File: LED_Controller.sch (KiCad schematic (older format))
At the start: 27 parts, among them CON1 CONNECTOR, CON2 CONNECTOR, CON3 CONNECTOR, CON4 CONNECTOR, CON5 PWR_CON, CON6 AVR-ISP-10, CON7 AVR-ISP-6, IC1 ATMEGA328P-P, Q1 STS8DN3LLH5, Q2 STS8DN3LLH5, Q3 STS8DN3LLH5

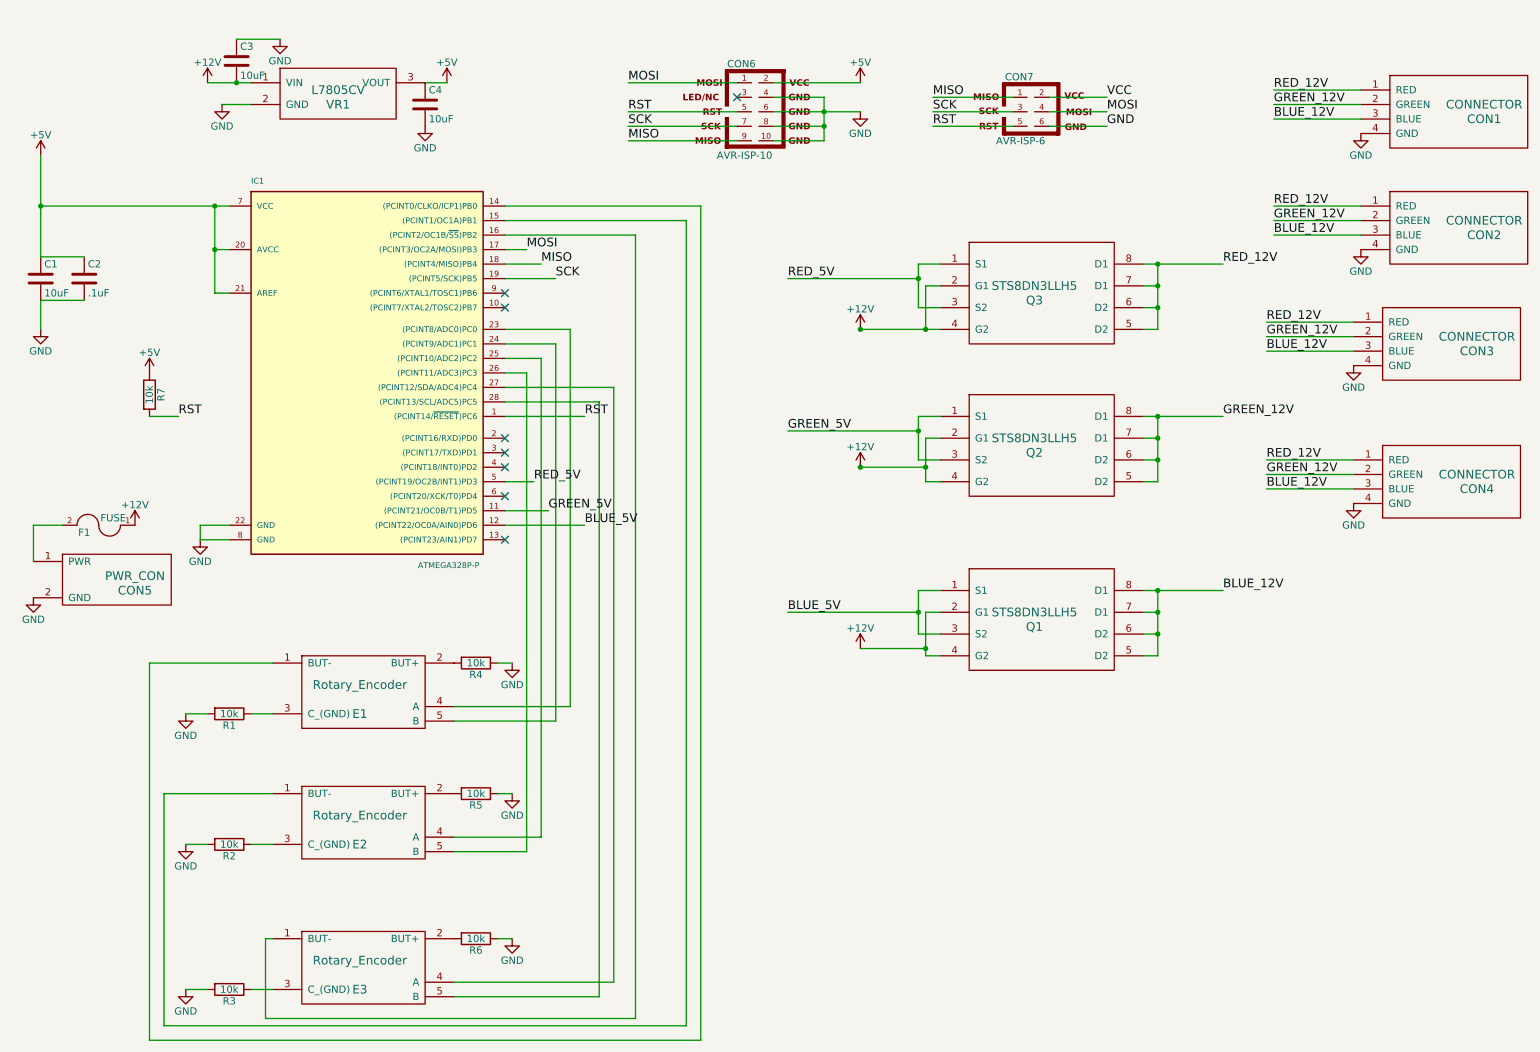
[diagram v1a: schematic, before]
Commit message: Changed to Common Anode, new status LEDs
Updated schematic to reflect common anode LED strip, instead of common
cathode.

Added indicator LEDs to 12V and 5V power supply.

Other minor routing changes. Still need to update footprint to make
rotary encoder pins larger and probably change the Atmega footprint to
the correct size.
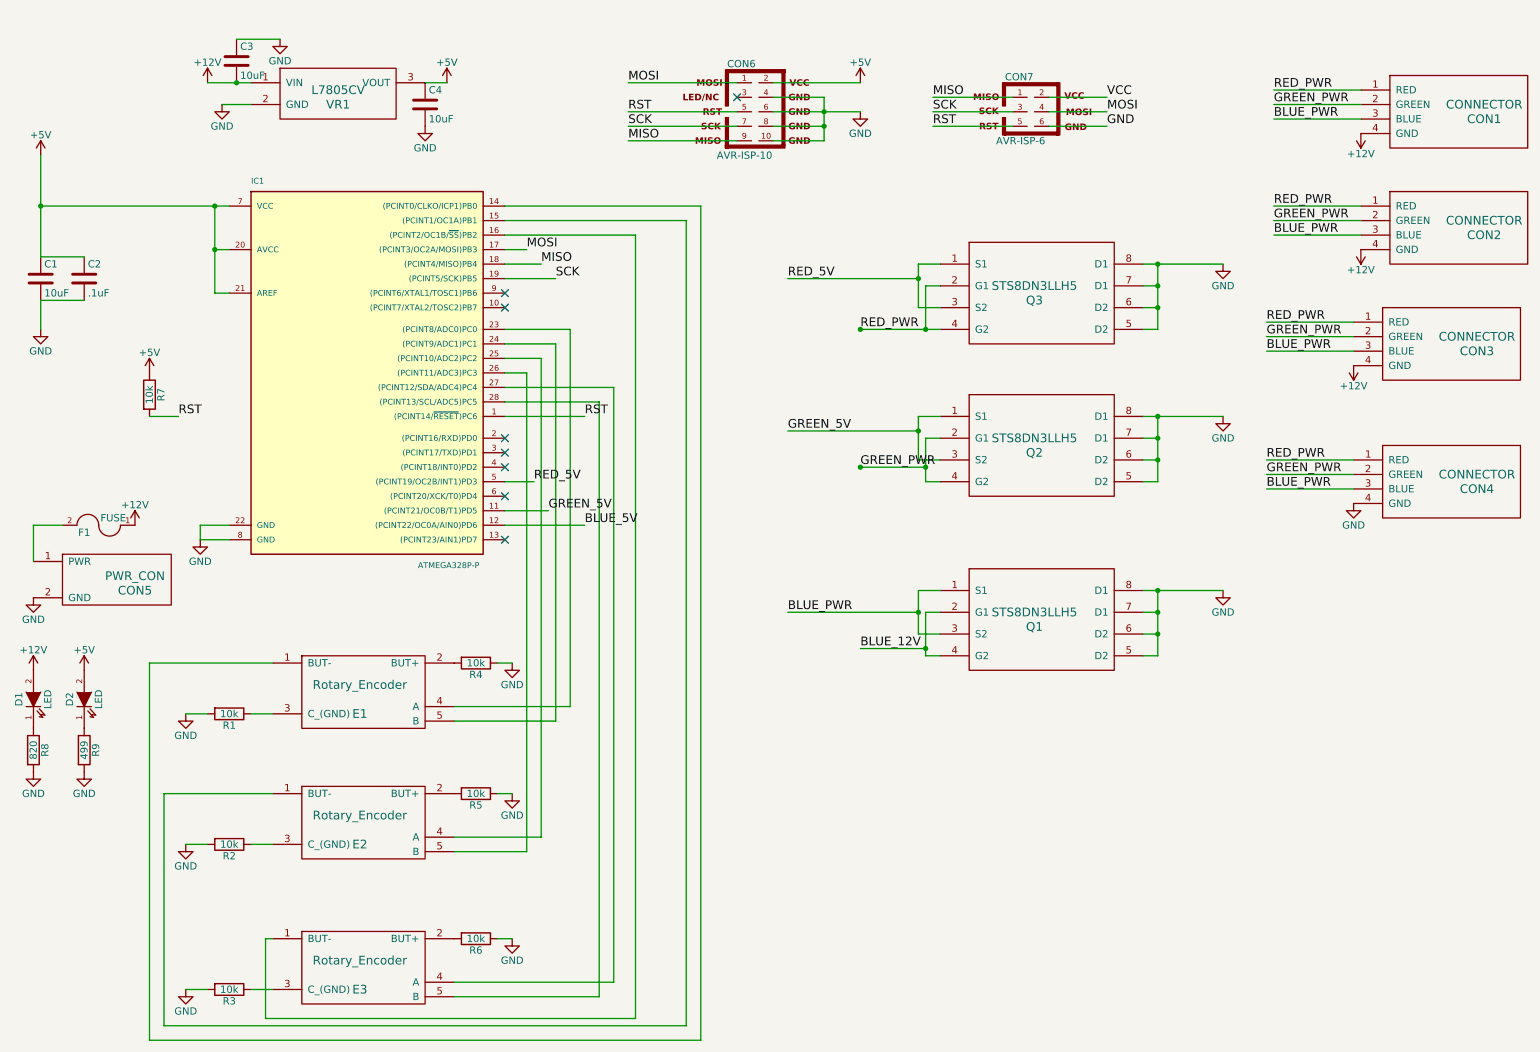
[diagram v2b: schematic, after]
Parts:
- added D1, D2: LED, LEDs:LED-3MM, symbol LED
- added R8: 820, LEDs:LED_1206, symbol R
- added R9: 499, LEDs:LED_1206, symbol R
- F1: footprint (none) -> LED_controller_footprints:12V_PWR_HOLES
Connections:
- net +12V: now also CON1.4 (GND), CON2.4 (GND), CON3.4 (GND), D1.2 (A); no longer Q1.2 (G1), Q1.4 (G2), Q2.2 (G1), Q2.4 (G2), Q3.2 (G1), Q3.4 (G2)
- net +5V: now also D2.2 (A)
- net BLUE_12V: now also Q1.2 (G1), Q1.4 (G2); no longer CON1.3 (BLUE), CON2.3 (BLUE), CON3.3 (BLUE), CON4.3 (BLUE), Q1.5 (D2), Q1.6 (D2), Q1.7 (D1), Q1.8 (D1)
- net BLUE_5V: no longer Q1.1 (S1), Q1.3 (S2)
- net GND: now also Q1.5 (D2), Q1.6 (D2), Q1.7 (D1), Q1.8 (D1), Q2.5 (D2), Q2.6 (D2), Q2.7 (D1), Q2.8 (D1), Q3.5 (D2), Q3.6 (D2), Q3.7 (D1), Q3.8 (D1), R8.2, R9.2; no longer CON1.4 (GND), CON2.4 (GND), CON3.4 (GND)
- net GREEN_12V renamed GREEN_PWR
- net GREEN_PWR: now also Q2.2 (G1), Q2.4 (G2); no longer Q2.5 (D2), Q2.6 (D2), Q2.7 (D1), Q2.8 (D1)
- net RED_12V renamed RED_PWR
- net RED_PWR: now also Q3.2 (G1), Q3.4 (G2); no longer Q3.5 (D2), Q3.6 (D2), Q3.7 (D1), Q3.8 (D1)
- new net: D1.1 (K), R8.1
- new net: D2.1 (K), R9.1
- new net BLUE_PWR: CON1.3 (BLUE), CON2.3 (BLUE), CON3.3 (BLUE), CON4.3 (BLUE), Q1.1 (S1), Q1.3 (S2)
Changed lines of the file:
@@
 BLUE_5V
 Text Label 5900 4650 0    60   ~ 0
-BLUE_5V
+BLUE_PWR
 Text Label 4250 3950 0    60   ~ 0
 GREEN_5V
@@
 	1    0    0    -1
 $EndComp
-$Comp
-L GND #PWR016
-U 1 1 56B7C77B
-P 9850 1350
-F 0 "#PWR016" H 9850 1100 50  0001 C CNN
-F 1 "GND" H 9850 1200 50  0000 C CNN
-F 2 "" H 9850 1350 60  0000 C CNN
-F 3 "" H 9850 1350 60  0000 C CNN
-	1    9850 1350
-	1    0    0    -1
-$EndComp
 Text Label 9250 1050 0    60   ~ 0
-RED_12V
+RED_PWR
 Text Label 9250 1150 0    60   ~ 0
-GREEN_12V
+GREEN_PWR
 Text Label 9250 1250 0    60   ~ 0
-BLUE_12V
+BLUE_PWR
 $Comp
 L CONNECTOR CON2
@@
 $EndComp
 Text Label 9250 1850 0    60   ~ 0
-RED_12V
+RED_PWR
 Text Label 9250 1950 0    60   ~ 0
-GREEN_12V
+GREEN_PWR
 Text Label 9250 2050 0    60   ~ 0
-BLUE_12V
+BLUE_PWR
 Text Label 4500 3300 0    60   ~ 0
 RST
@@
 $EndComp
 Text Label 9200 2650 0    60   ~ 0
-RED_12V
+RED_PWR
 Text Label 9200 2750 0    60   ~ 0
-GREEN_12V
+GREEN_PWR
 Text Label 9200 2850 0    60   ~ 0
-BLUE_12V
+BLUE_PWR
 $Comp
 L CONNECTOR CON4
@@
 $EndComp
 $Comp
-L GND #PWR017
+L GND #PWR016
 U 1 1 56B7D40D
 P 9800 3900
-F 0 "#PWR017" H 9800 3650 50  0001 C CNN
+F 0 "#PWR016" H 9800 3650 50  0001 C CNN
 F 1 "GND" H 9800 3750 50  0000 C CNN
 F 2 "" H 9800 3900 60  0000 C CNN
@@
 $EndComp
 Text Label 9200 3600 0    60   ~ 0
-RED_12V
+RED_PWR
 Text Label 9200 3700 0    60   ~ 0
-GREEN_12V
+GREEN_PWR
 Text Label 9200 3800 0    60   ~ 0
-BLUE_12V
-Text Label 8900 2250 0    60   ~ 0
-RED_12V
-Text Label 8900 3300 0    60   ~ 0
-GREEN_12V
-Text Label 8900 4500 0    60   ~ 0
+BLUE_PWR
+Text Label 6400 2700 0    60   ~ 0
+RED_PWR
+Text Label 6400 3650 0    60   ~ 0
+GREEN_PWR
+Text Label 6400 4900 0    60   ~ 0
 BLUE_12V
 NoConn ~ 5550 1100
 $Comp
-L +12V #PWR018
-U 1 1 56B7FECA
-P 6400 3650
-F 0 "#PWR018" H 6400 3500 50  0001 C CNN
-F 1 "+12V" H 6400 3790 50  0000 C CNN
-F 2 "" H 6400 3650 60  0000 C CNN
-F 3 "" H 6400 3650 60  0000 C CNN
-	1    6400 3650
-	1    0    0    -1
-$EndComp
-$Comp
-L +12V #PWR019
-U 1 1 56B7FF1D
-P 6400 4900
-F 0 "#PWR019" H 6400 4750 50  0001 C CNN
-F 1 "+12V" H 6400 5040 50  0000 C CNN
-F 2 "" H 6400 4900 60  0000 C CNN
-F 3 "" H 6400 4900 60  0000 C CNN
-	1    6400 4900
-	1    0    0    -1
-$EndComp
-$Comp
-L GND #PWR020
+L GND #PWR017
 U 1 1 56B801F8
 P 2400 700
-F 0 "#PWR020" H 2400 450 50  0001 C CNN
+F 0 "#PWR017" H 2400 450 50  0001 C CNN
 F 1 "GND" H 2400 550 50  0000 C CNN
 F 2 "" H 2400 700 60  0000 C CNN
 F 3 "" H 2400 700 60  0000 C CNN
 	1    2400 700
-	1    0    0    -1
-$EndComp
-$Comp
-L GND #PWR021
-U 1 1 56B80FD6
-P 9850 2150
-F 0 "#PWR021" H 9850 1900 50  0001 C CNN
-F 1 "GND" H 9850 2000 50  0000 C CNN
-F 2 "" H 9850 2150 60  0000 C CNN
-F 3 "" H 9850 2150 60  0000 C CNN
-	1    9850 2150
-	1    0    0    -1
-$EndComp
-$Comp
-L GND #PWR022
-U 1 1 56B8118A
-P 9800 2950
-F 0 "#PWR022" H 9800 2700 50  0001 C CNN
-F 1 "GND" H 9800 2800 50  0000 C CNN
-F 2 "" H 9800 2950 60  0000 C CNN
-F 3 "" H 9800 2950 60  0000 C CNN
-	1    9800 2950
 	1    0    0    -1
 $EndComp
@@
 Connection ~ 2100 1000
 $Comp
-L +12V #PWR023
+L +12V #PWR018
 U 1 1 56BAC237
 P 1900 1000
-F 0 "#PWR023" H 1900 850 50  0001 C CNN
+F 0 "#PWR018" H 1900 850 50  0001 C CNN
 F 1 "+12V" H 1900 1140 50  0000 C CNN
 F 2 "" H 1900 1000 60  0000 C CNN
 F 3 "" H 1900 1000 60  0000 C CNN
 	1    1900 1000
-	1    0    0    -1
-$EndComp
-$Comp
-L +12V #PWR024
-U 1 1 56BAC558
-P 6400 2700
-F 0 "#PWR024" H 6400 2550 50  0001 C CNN
-F 1 "+12V" H 6400 2840 50  0000 C CNN
-F 2 "" H 6400 2700 60  0000 C CNN
-F 3 "" H 6400 2700 60  0000 C CNN
-	1    6400 2700
 	1    0    0    -1
 $EndComp
@@
 F 0 "F1" H 1250 4100 50  0000 C CNN
 F 1 "FUSE" H 1050 4000 50  0000 C CNN
-F 2 "" H 1150 4050 60  0001 C CNN
+F 2 "LED_controller_footprints:12V_PWR_HOLES" H 1150 4050 60  0001 C CNN
 F 3 "" H 1150 4050 60  0000 C CNN
 	1    1150 4050
@@
 $EndComp
 Wire Wire Line
-	700  4300 700  4050
-Wire Wire Line
 	700  4050 900  4050
 $Comp
-L +12V #PWR025
+L +12V #PWR019
 U 1 1 56BE5D46
 P 1400 4050
-F 0 "#PWR025" H 1400 3900 50  0001 C CNN
+F 0 "#PWR019" H 1400 3900 50  0001 C CNN
 F 1 "+12V" H 1400 4190 50  0000 C CNN
 F 2 "" H 1400 4050 60  0000 C CNN
@@
 $EndComp
 $Comp
-L +5V #PWR026
+L +5V #PWR020
 U 1 1 56C11944
 P 1500 3000
-F 0 "#PWR026" H 1500 2850 50  0001 C CNN
+F 0 "#PWR020" H 1500 2850 50  0001 C CNN
 F 1 "+5V" H 1500 3140 50  0000 C CNN
 F 2 "" H 1500 3000 60  0000 C CNN
@@
 Wire Wire Line
 	1500 3300 1700 3300
+$Comp
+L +12V #PWR021
+U 1 1 56C4D7F9
+P 9850 1350
+F 0 "#PWR021" H 9850 1200 50  0001 C CNN
+F 1 "+12V" H 9850 1490 50  0000 C CNN
+F 2 "" H 9850 1350 60  0000 C CNN
+F 3 "" H 9850 1350 60  0000 C CNN
+	1    9850 1350
+	-1   0    0    1
+$EndComp
+$Comp
+L +12V #PWR022
+U 1 1 56C4D85C
+P 9850 2150
+F 0 "#PWR022" H 9850 2000 50  0001 C CNN
+F 1 "+12V" H 9850 2290 50  0000 C CNN
+F 2 "" H 9850 2150 60  0000 C CNN
+F 3 "" H 9850 2150 60  0000 C CNN
+	1    9850 2150
+	-1   0    0    1
+$EndComp
+$Comp
+L +12V #PWR023
+U 1 1 56C4D8B8
+P 9800 2950
+F 0 "#PWR023" H 9800 2800 50  0001 C CNN
+F 1 "+12V" H 9800 3090 50  0000 C CNN
+F 2 "" H 9800 2950 60  0000 C CNN
+F 3 "" H 9800 2950 60  0000 C CNN
+	1    9800 2950
+	-1   0    0    1
+$EndComp
+$Comp
+L GND #PWR024
+U 1 1 56C4DFDF
+P 8900 2250
+F 0 "#PWR024" H 8900 2000 50  0001 C CNN
+F 1 "GND" H 8900 2100 50  0000 C CNN
+F 2 "" H 8900 2250 60  0000 C CNN
+F 3 "" H 8900 2250 60  0000 C CNN
+	1    8900 2250
+	1    0    0    -1
+$EndComp
+$Comp
+L GND #PWR025
+U 1 1 56C4E044
+P 8900 3300
+F 0 "#PWR025" H 8900 3050 50  0001 C CNN
+F 1 "GND" H 8900 3150 50  0000 C CNN
+F 2 "" H 8900 3300 60  0000 C CNN
+F 3 "" H 8900 3300 60  0000 C CNN
+	1    8900 3300
+	1    0    0    -1
+$EndComp
+$Comp
+L GND #PWR026
+U 1 1 56C4E0A9
+P 8900 4500
+F 0 "#PWR026" H 8900 4250 50  0001 C CNN
+F 1 "GND" H 8900 4350 50  0000 C CNN
+F 2 "" H 8900 4500 60  0000 C CNN
+F 3 "" H 8900 4500 60  0000 C CNN
+	1    8900 4500
+	1    0    0    -1
+$EndComp
+$Comp
+L +12V #PWR027
+U 1 1 56C51D4A
+P 700 5050
+F 0 "#PWR027" H 700 4900 50  0001 C CNN
+F 1 "+12V" H 700 5190 50  0000 C CNN
+F 2 "" H 700 5050 60  0000 C CNN
+F 3 "" H 700 5050 60  0000 C CNN
+	1    700  5050
+	1    0    0    -1
+$EndComp
+$Comp
+L LED D1
+U 1 1 56C51FB0
+P 700 5250
+F 0 "D1" H 700 5350 50  0000 C CNN
+F 1 "LED" H 700 5150 50  0000 C CNN
+F 2 "LEDs:LED-3MM" H 700 5250 60  0001 C CNN
+F 3 "" H 700 5250 60  0000 C CNN
+	1    700  5250
+	0    -1   -1   0
+$EndComp
+$Comp
+L GND #PWR028
+U 1 1 56C5202B
+P 700 5750
+F 0 "#PWR028" H 700 5500 50  0001 C CNN
+F 1 "GND" H 700 5600 50  0000 C CNN
+F 2 "" H 700 5750 60  0000 C CNN
+F 3 "" H 700 5750 60  0000 C CNN
+	1    700  5750
+	1    0    0    -1
+$EndComp
+$Comp
+L +5V #PWR029
+U 1 1 56C52093
+P 1050 5050
+F 0 "#PWR029" H 1050 4900 50  0001 C CNN
+F 1 "+5V" H 1050 5190 50  0000 C CNN
+F 2 "" H 1050 5050 60  0000 C CNN
+F 3 "" H 1050 5050 60  0000 C CNN
+	1    1050 5050
+	1    0    0    -1
+$EndComp
+$Comp
+L LED D2
+U 1 1 56C520F9
+P 1050 5250
+F 0 "D2" H 1050 5350 50  0000 C CNN
+F 1 "LED" H 1050 5150 50  0000 C CNN
+F 2 "LEDs:LED-3MM" H 1050 5250 60  0001 C CNN
+F 3 "" H 1050 5250 60  0000 C CNN
+	1    1050 5250
+	0    -1   -1   0
+$EndComp
+$Comp
+L R R8
+U 1 1 56C521C8
+P 700 5600
+F 0 "R8" V 780 5600 50  0000 C CNN
+F 1 "820" V 700 5600 50  0000 C CNN
+F 2 "LEDs:LED_1206" V 630 5600 30  0001 C CNN
+F 3 "" H 700 5600 30  0000 C CNN
+	1    700  5600
+	1    0    0    -1
+$EndComp
+$Comp
+L R R9
+U 1 1 56C5231F
+P 1050 5600
+F 0 "R9" V 1130 5600 50  0000 C CNN
+F 1 "499" V 1050 5600 50  0000 C CNN
+F 2 "LEDs:LED_1206" V 980 5600 30  0001 C CNN
+F 3 "" H 1050 5600 30  0000 C CNN
+	1    1050 5600
+	1    0    0    -1
+$EndComp
+$Comp
+L GND #PWR030
+U 1 1 56C52394
+P 1050 5750
+F 0 "#PWR030" H 1050 5500 50  0001 C CNN
+F 1 "GND" H 1050 5600 50  0000 C CNN
+F 2 "" H 1050 5750 60  0000 C CNN
+F 3 "" H 1050 5750 60  0000 C CNN
+	1    1050 5750
+	1    0    0    -1
+$EndComp
+Wire Wire Line
+	700  4050 700  4300
 $EndSCHEMATC
